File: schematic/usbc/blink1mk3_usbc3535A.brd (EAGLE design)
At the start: 16 x 10 mm, 19 parts, among them J1 DX07P024AJ1R1500, T0A TPTP10R, T1B TPTP10R, U1 EFM32HG309F64G

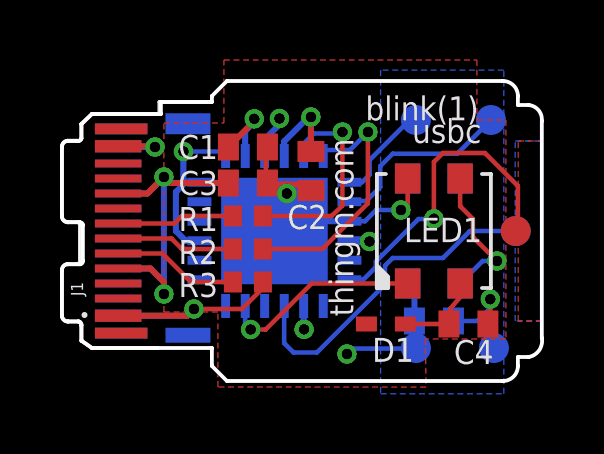
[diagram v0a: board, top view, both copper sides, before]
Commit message: update usbc3535A board
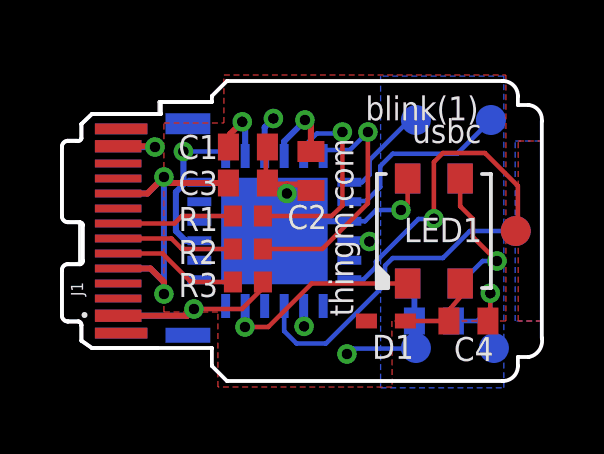
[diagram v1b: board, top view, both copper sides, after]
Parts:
- moved C4 0.10 mm to (8.75, -3.00)
- moved D1 0.10 mm to (6.05, -3.00)
